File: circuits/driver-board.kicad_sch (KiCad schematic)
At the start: 72 parts, among them J1 Conn_01x18_Female, J2 USB4120-03-C_REVA, J3 Motor_Conn_01x04, J4 Screw_Terminals, J5 Conn_01x06_Female, Q1 SS8050-G, Q2 SS8050-G, SW1 RST_SW_Push, U1 CP2102N-Axx-xQFN24, U2 BA33DD0T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

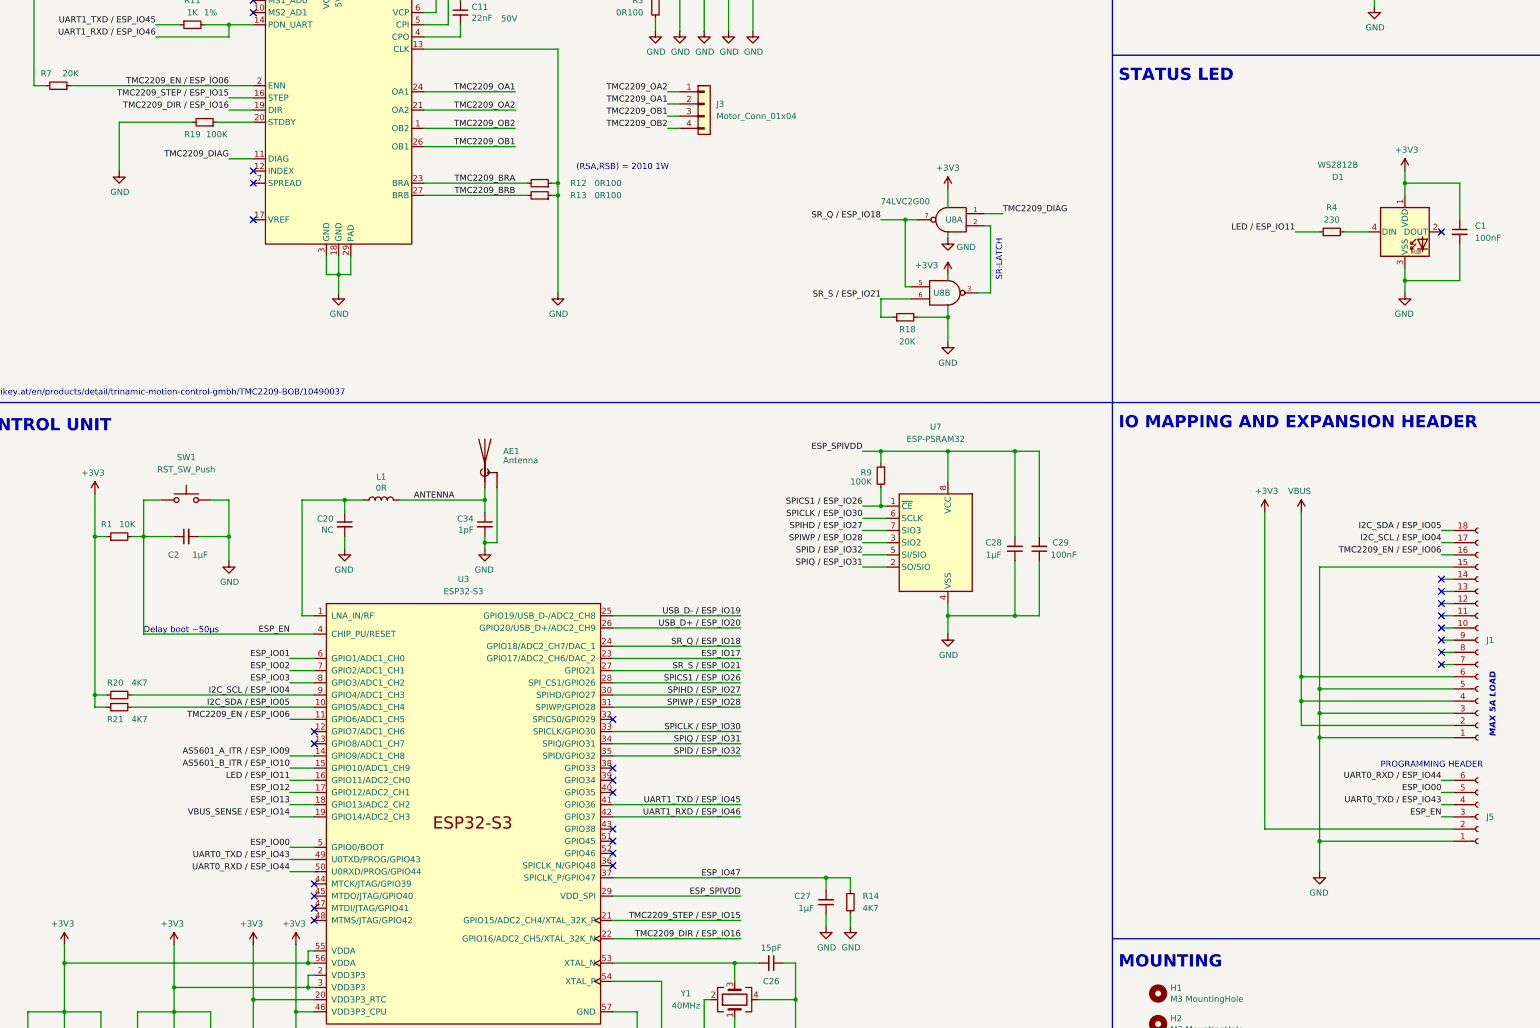
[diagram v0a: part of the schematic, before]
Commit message: changed gpio for step/dir
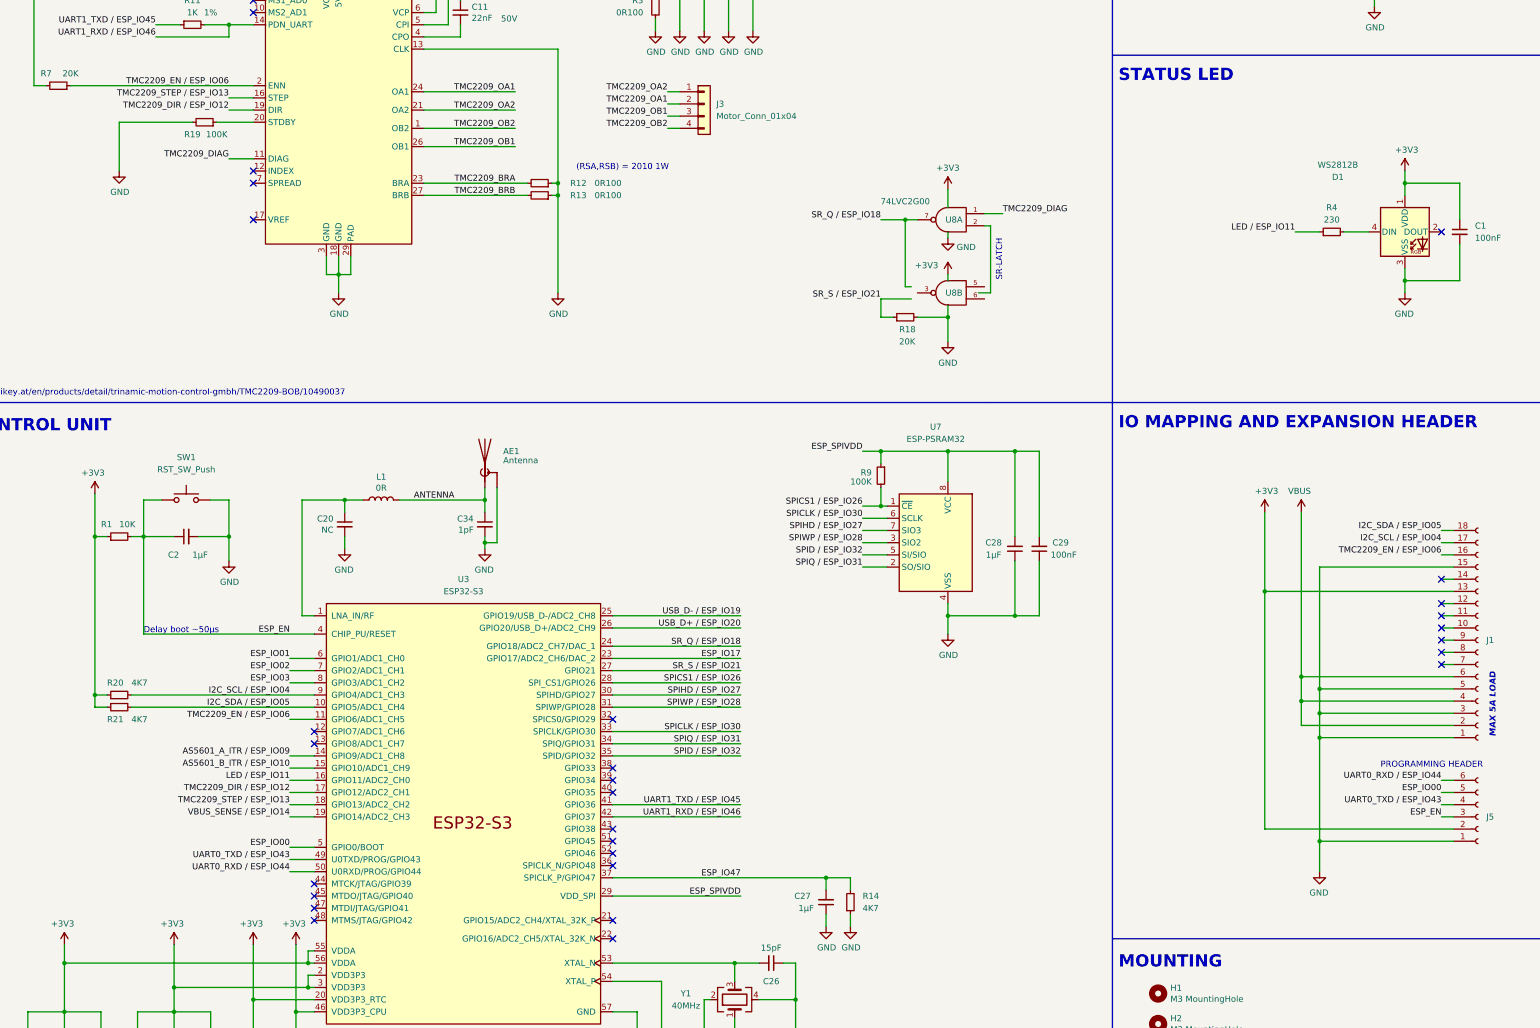
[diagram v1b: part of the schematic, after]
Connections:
- net +3V3: now also J1.13 (Pin_13)
- net SR_Q / ESP_IO18: no longer U8.5
- net SR_S / ESP_IO21: no longer U8.6
- net at U8.3: no longer U8.2
- net ESP_IO12 renamed TMC2209_DIR / ESP_IO12
- net TMC2209_DIR / ESP_IO12: now also U5.19 (DIR)
- net ESP_IO13 renamed TMC2209_STEP / ESP_IO13
- net TMC2209_STEP / ESP_IO13: now also U5.16 (STEP)
- net TMC2209_DIR / ESP_IO16: no longer names the net of U3.22 (GPIO16/ADC2_CH5/XTAL_32K_N)
- net TMC2209_DIR / ESP_IO16: no longer U5.19 (DIR)
- net TMC2209_STEP / ESP_IO15: no longer names the net of U3.21 (GPIO15/ADC2_CH4/XTAL_32K_P)
- net TMC2209_STEP / ESP_IO15: no longer U5.16 (STEP)
- no-connect marks 56 -> 57
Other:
- moved on the sheet: U8B

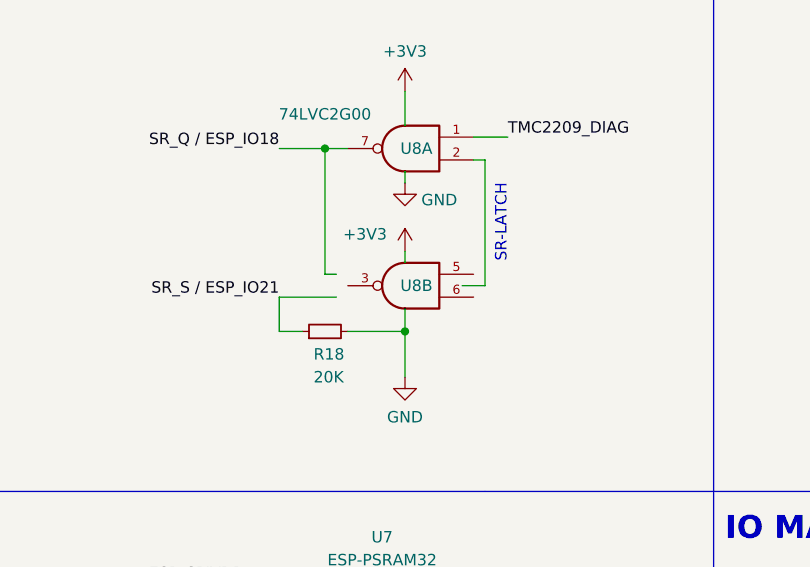
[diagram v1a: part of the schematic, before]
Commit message: flipped symbol
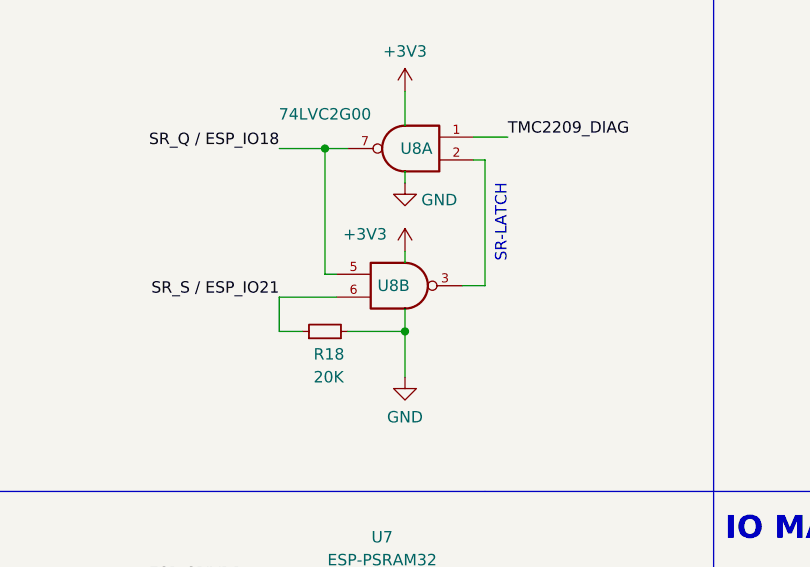
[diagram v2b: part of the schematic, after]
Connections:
- net SR_Q / ESP_IO18: now also U8.5
- net SR_S / ESP_IO21: now also U8.6
- net at U8.3: now also U8.2
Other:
- moved on the sheet: U8B
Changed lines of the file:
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@@
     (pin "2")
   )
-  (symbol (lib_id "74xGxx:74LVC2G00") (at 372.11 129.54 0) (mirror y) (unit 2)
+  (symbol (lib_id "74xGxx:74LVC2G00") (at 372.11 129.54 0) (unit 2)
     (in_bom yes) (on_board yes)
-    (property "Reference" "U8" (id 0) (at 373.38 129.54 0))
-    (property "Value" "74LVC2G00" (id 1) (at 373.38 120.65 0)
+    (property "Reference" "U8" (id 0) (at 370.84 129.54 0))
+    (property "Value" "74LVC2G00" (id 1) (at 370.84 120.65 0)
       (effects (font (size 1.27 1.27)) hide)
     )

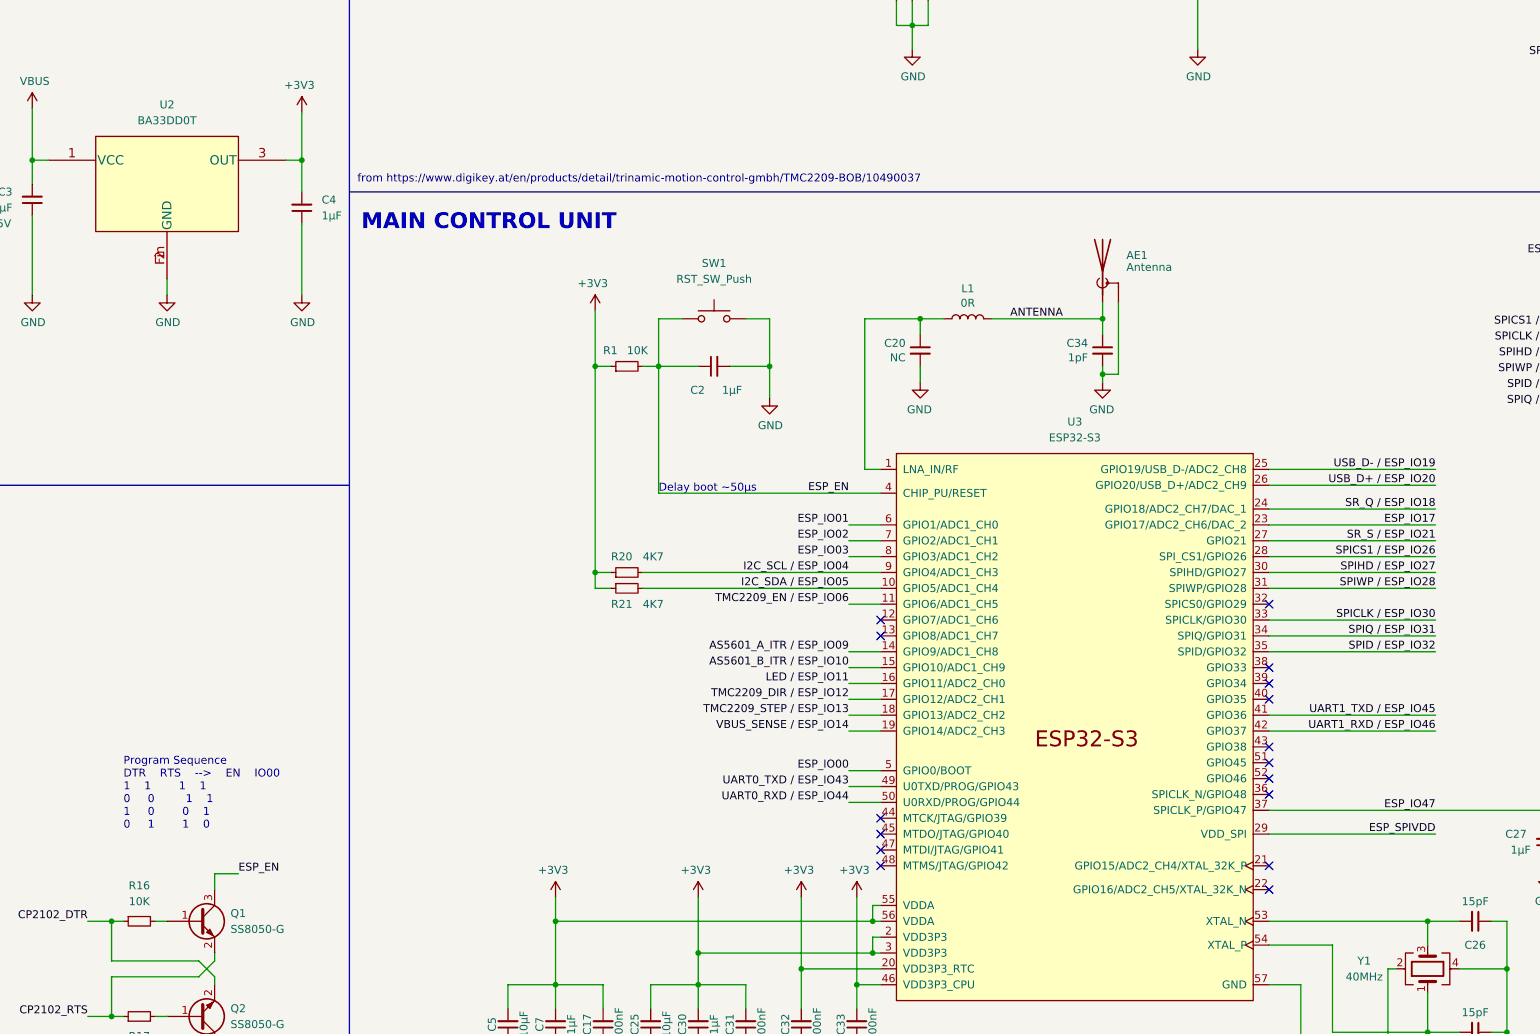
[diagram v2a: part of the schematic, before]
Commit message: added info for BOM; redid some traces and labels
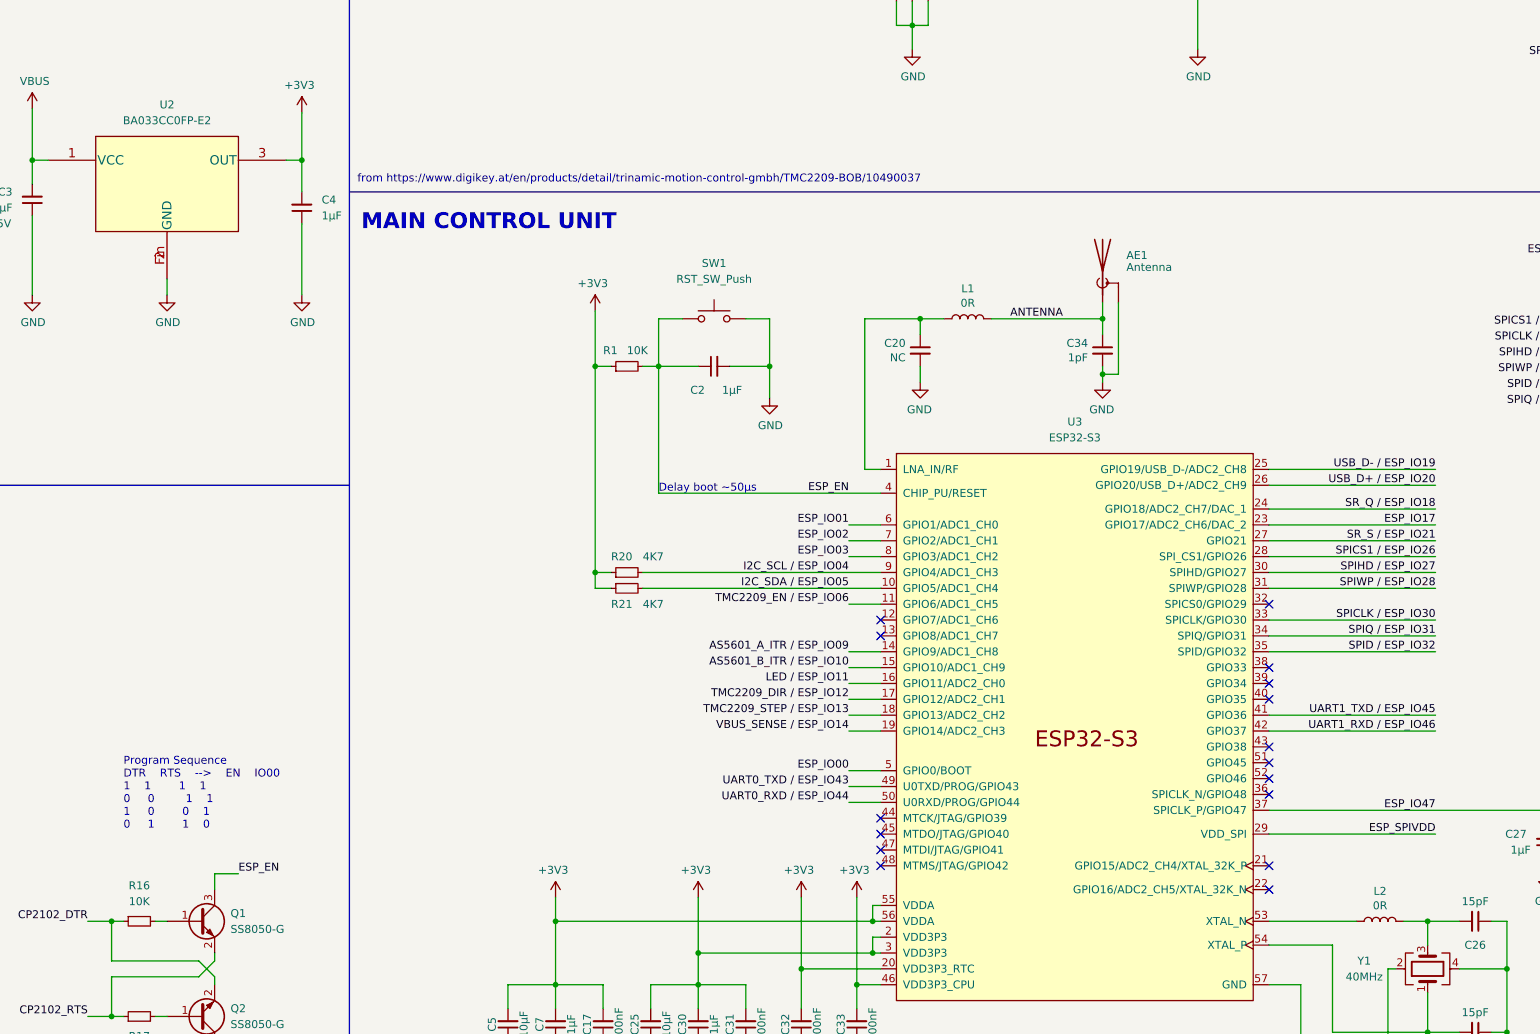
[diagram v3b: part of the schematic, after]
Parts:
- added L2: 0R, Resistor_SMD:R_0201_0603Metric, symbol Device:L
- AE1: digikey_part_number (none) -> 2115-NN01-102CT-ND; mfr_part_number (none) -> NN01-102
- D1: lcsc_part_number (none) -> C965555; mfr_part_number (none) -> WS2812B-2020
- D3: digikey_part_number (none) -> 2156-P6SMB24AT3G-ND; mfr_part_number (none) -> P6SMB24AT3G
- J2: digikey_part_number (none) -> 2073-USB4120-03-CCT-ND; mfr_part_number (none) -> USB4120-03-C
- J3: digikey_part_number (none) -> 455-1613-ND; mfr_part_number (none) -> B4B-EH-A(LF)(SN)
- Q1, Q2: digikey_part_number (none) -> 641-1790-1-ND; mfr_part_number (none) -> SS8050-G
- R1, R19, R4, R7: footprint Resistor_SMD:R_0201_0603Metric -> Resistor_SMD:R_0402_1005Metric
- SW1: digikey_part_number (none) -> SW1020CT-ND; mfr_part_number (none) -> B3U-1000P
- U1: digikey_part_number (none) -> 336-5888-1-ND; mfr_part_number (none) -> CP2102N-A02-GQFN24R
- U2: value BA33DD0T -> BA033CC0FP-E2; digikey_part_number (none) -> BA033CC0FP-E2CT-ND; mfr_part_number (none) -> BA033CC0FP-E2
- U3: digikey_part_number (none) -> 1965-ESP32-S3-ND
- U4: digikey_part_number (none) -> AS5601-ASOTCT-ND; mfr_part_number (none) -> AS5601-ASOT
- U5: mfr_part_number (none) -> TMC2209-LA
- U6: digikey_part_number (none) -> 497-18060-1-ND; mfr_part_number (none) -> STUSB4500QTR
- U8: digikey_part_number (none) -> 296-SN74LVC2G00DCT3CT-ND; mft_part_number (none) -> SN74LVC2G00DCT3
- Y1: digikey_part_number (none) -> 490-5586-1-ND; mfr_part_number (none) -> XRCGB40M000F4M00R0
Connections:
- net at C26.2, Y1.3: now also L2.1; no longer U3.53 (XTAL_N)
- new net: L2.2, U3.53 (XTAL_N)
